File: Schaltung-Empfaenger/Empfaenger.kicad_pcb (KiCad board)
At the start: 2 copper layers, 44 parts, among them J1 Conn_01x06 USB, J2 Poti 47k, J3 Poti 47k, J4 Poti 47k, J5 BTN, J6 Fan, J7 LED Stripe, J8 Piezo Transducter 12V, Q1 IRLML9301, Q2 2N7002, Q3 BC337, U1 L7805, U2 CH224K, U3 XIAO ESP32C3, U4 TSR0.5-2433, U5 74AHCT1G125

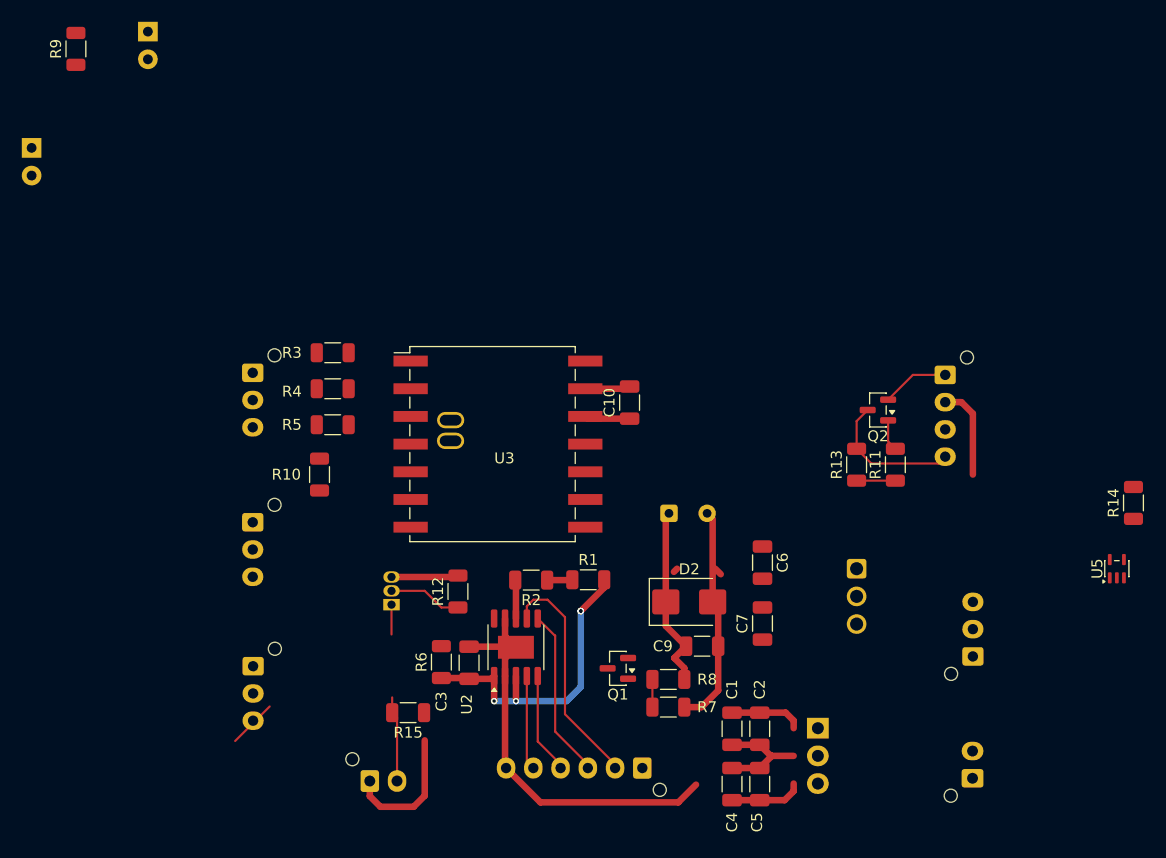
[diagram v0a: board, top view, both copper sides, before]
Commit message: Empfaenger: PCB fertig geroutet
Layout des Empfaenger-Boards abgeschlossen.

PCB
- Leiterbahnen 100 -> 323 Segmente, Vias 4 -> 10: das Board ist jetzt
  durchgeroutet statt teilverdrahtet
- Zweite Kupferflaeche hinzugekommen (1 -> 2 Zonen)
- Platinenumriss gezeichnet (4 gr_line)
- C11 platziert (44 -> 45 Footprints)

Schaltplan
- C11 (1µF, 1206) und die Versorgung VDD_PD ergaenzt, dazu zwei
  Power-Symbole (#PWR052/053) sowie 2k2 und 470 Ohm
- 14 Widerstaende von 1206 auf 0603 umgestellt

Die Netz-Labels sind unveraendert — der Pin-Contract aus
specs/004-v3-esp32-port/contracts/hardware-pins.md gilt weiter, die
Empfaenger-Firmware ist von dieser Aenderung nicht betroffen.

Co-Authored-By: Claude Opus 5 (1M context) <noreply@anthropic.com>
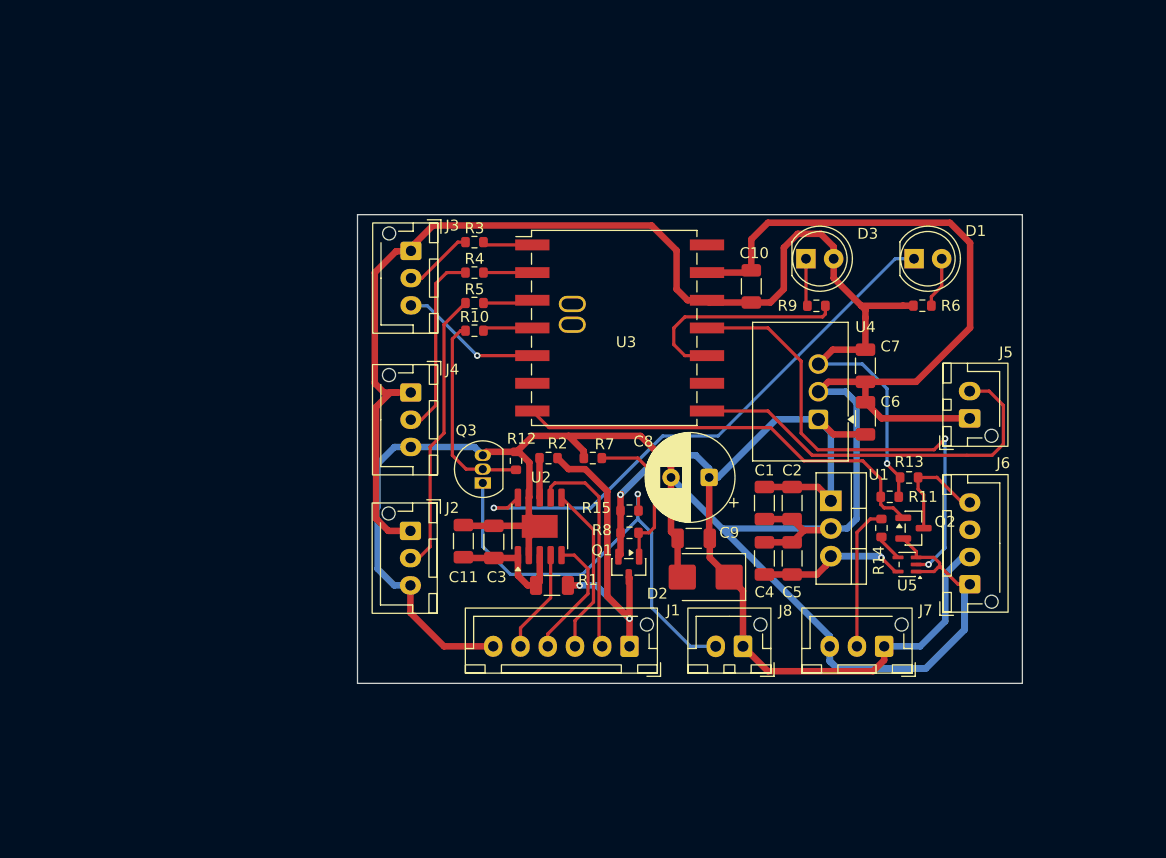
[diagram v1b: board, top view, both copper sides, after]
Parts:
- added C11: 1µF, Capacitor_SMD:C_1206_3216Metric, F.Cu at (77.7, 154.9)
- C8, D1, D3, J1, J2, J3, J4, J5, J6, J7, J8, Q3, U1, U4: moved to F.Cu
- R10, R11, R12, R13, R14, R2, R3, R4, R5, R6, R7, R8, R9: footprint Resistor_SMD:R_1206_3216Metric -> Resistor_SMD:R_0603_1608Metric
- R15: value 470 -> 2k2; footprint Resistor_SMD:R_1206_3216Metric -> Resistor_SMD:R_0603_1608Metric
- moved D1 81.6 mm to (119.1, 129.0), turned to 0 degrees
- moved R9 71.9 mm to (110.1, 133.4), turned to 180 degrees
- moved D3 63.9 mm to (109.1, 129.0), turned to 0 degrees
- moved R6 54.9 mm to (119.8, 133.3), turned to 0 degrees
- moved J8 36.4 mm to (103.4, 164.6), turned to 180 degrees
- moved J5 33.0 mm to (124.2, 143.7)
- moved R15 27.5 mm to (93.0, 152.2), turned to 0 degrees
- moved C7 25.5 mm to (114.6, 138.9), turned to -90 degrees
- moved R7 23.9 mm to (89.6, 147.3), turned to 180 degrees
- moved R14 23.2 mm to (116.1, 153.7)
- moved C1 20.9 mm to (105.3, 151.5)
- moved C2 20.9 mm to (107.9, 151.5)
- moved C4 20.9 mm to (105.3, 156.5)
- moved C5 20.9 mm to (107.9, 156.5)
- moved U1 20.9 mm to (111.4, 151.3)
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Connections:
- C3 pad 1: +3V3 -> VDD_PD
- R1 pad 2: +3V3 -> VDD_PD
- U2 pad 1: +3V3 -> VDD_PD
- U2 pad 3: +3V3 -> VDD_PD
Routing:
- net GND: track 89.8 -> 240.2 mm
- net +3V3: track 36.4 -> 123.1 mm, vias 4 -> 1
- net +12V: track 44.5 -> 94.9 mm, vias 0 -> 1
- net Net-(D1-K): track 0.00 -> 50.1 mm, vias 0 -> 1
- net /<NO NET>: track 0.00 -> 44.1 mm, vias 0 -> 2
- net /SIG_FAN: track 2.88 -> 39.5 mm
- net /BTN: track 0.00 -> 36.5 mm
- net Net-(J8-Pin_2): track 10.6 -> 43.1 mm, vias 0 -> 1
- net VBUS: track 2.24 -> 31.6 mm, vias 0 -> 2
- net Net-(J2-Pin_2): track 0.00 -> 25.9 mm
- net Net-(U3-D9): track 0.00 -> 20.2 mm
- net Net-(J4-Pin_2): track 0.00 -> 17.2 mm
- net Net-(J7-Pin_2): track 0.00 -> 13.2 mm
- net /GND_POTI: track 0.00 -> 13.0 mm, vias 0 -> 1
- net Net-(Q3-B): track 6.73 -> 18.8 mm
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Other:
- board outline added: 61 x 43 mm
